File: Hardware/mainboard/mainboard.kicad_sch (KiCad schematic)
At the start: 85 parts, among them IC1 DS1813, IC2 DS1813, J1 Barrel_Jack, J2 Conn_02x02_Odd_Even, J3 Conn_01x06, J4 Conn_01x14, SW1 SW, U1 74AC161, U2 L7905, U4 PAL24, U5 GAL16V8, U6 W65C02SxP, U7 HM62256BLP, U8 28C256, U9 W65C51NxP, X1 24MHz, X3 1.8432MHz

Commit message: Fix mainboard power + add A13 and A14 to RAM/ROM address decoding.
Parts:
- removed U2: L7905, Package_TO_SOT_THT:TO-220-3_Vertical, symbol Regulator_Linear:L7905
- added C3, C4: .1u, Capacitor_THT:C_Disc_D4.3mm_W1.9mm_P5.00mm, symbol Device:C_Small
- added C5: 47u, Capacitor_THT:CP_Radial_D4.0mm_P2.00mm, symbol Device:C_Small
- added U1: L7805, Package_TO_SOT_THT:TO-220-3_Vertical, symbol Regulator_Linear:L7805
- C1: renamed from C13; footprint Capacitor_THT:CP_Radial_D6.3mm_P2.50mm -> Capacitor_THT:CP_Radial_D4.0mm_P2.00mm
- C12: renamed from C6; value 47n -> 1u
- R25: renamed from R27; footprint Resistor_THT:R_Axial_DIN0204_L3.6mm_D1.6mm_P5.08mm_Horizontal -> Resistor_THT:R_Axial_DIN0207_L6.3mm_D2.5mm_P7.62mm_Horizontal
- U2: renamed from U4; value PAL24 -> AT22V10
- renumbered C16 to C10, C7 to C11, C4 to C13, C17 to C14, C12 to C15, C8 to C16, C2 to C17, C15 to C18, C5 to C19, C1 to C2, C9 to C20, C10 to C6, C3 to C7, C11 to C8, C14 to C9, D9 to D1, D1 to D3, D3 to D4, D4 to D5, D5 to D6, D6 to D7, D7 to D8, D8 to D9, H5 to H1, H6 to H2, H1 to H3, H2 to H4, H3 to H5, J3 to J2, J2 to J3, R10 to R1, R4 to R10, R5 to R11, R6 to R12, R14 to R13, R21 to R14, R22 to R15, R7 to R16, R16 to R17, R15 to R18, R24 to R19, R11 to R2, R25 to R20, R26 to R21, R17 to R22, R18 to R23, R23 to R24, R12 to R3, R13 to R4, R9 to R5, R1 to R6, R8 to R7, R2 to R8, R3 to R9, SLOT4 to SLOT1, SLOT0 to SLOT2, SLOT1 to SLOT3, SLOT5 to SLOT4, SLOT2 to SLOT5, SLOT3 to SLOT6, U9 to U3, U7 to U4, U1 to U5, U8 to U6, U5 to U7, U6 to U8, X3 to X2
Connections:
- net +5V: now also C4.1, C5.1, U1.3 (OUT); no longer C1.1
- net A13: now also U7.15 (IO5)
- net A14: now also U7.14 (IO6)
- net GND: now also C3.2, C4.2, C5.2, U1.2 (GND)
- net at D1.1 (K), SW1.1 (A): now also C1.1
- net at SW1.2 (B): now also C3.1, U1.1 (IN)
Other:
- moved on the sheet: C1

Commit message: Change slot solder mask
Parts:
- renumbered SLOT2 to SLOT0, SLOT3 to SLOT1, SLOT5 to SLOT2, SLOT6 to SLOT3, SLOT1 to SLOT4, SLOT4 to SLOT5
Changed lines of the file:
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@@
   (symbol (lib_id "Connector_Generic:Conn_02x25_Odd_Even") (at 172.72 91.44 0) (unit 1)
     (in_bom yes) (on_board yes)
-    (property "Reference" "SLOT5" (id 0) (at 173.99 55.4482 0))
+    (property "Reference" "SLOT2" (id 0) (at 173.99 55.4482 0))
     (property "Value" "Conn_01x40" (id 1) (at 173.99 57.7596 0))
     (property "Footprint" "Connector_PinSocket_2.54mm:PinSocket_2x25_P2.54mm_Vertical" (id 2) (at 172.72 91.44 0)
@@
   (symbol (lib_id "Connector_Generic:Conn_02x25_Odd_Even") (at 62.23 208.28 0) (unit 1)
     (in_bom yes) (on_board yes)
-    (property "Reference" "SLOT1" (id 0) (at 63.5 172.2882 0))
+    (property "Reference" "SLOT4" (id 0) (at 63.5 172.2882 0))
     (property "Value" "Conn_01x40" (id 1) (at 63.5 174.5996 0))
     (property "Footprint" "Connector_PinSocket_2.54mm:PinSocket_2x25_P2.54mm_Vertical" (id 2) (at 62.23 208.28 0)
@@
   (symbol (lib_id "Connector_Generic:Conn_02x25_Odd_Even") (at 118.11 209.55 0) (unit 1)
     (in_bom yes) (on_board yes)
-    (property "Reference" "SLOT4" (id 0) (at 119.38 173.5582 0))
+    (property "Reference" "SLOT5" (id 0) (at 119.38 173.5582 0))
     (property "Value" "Conn_01x40" (id 1) (at 119.38 175.8696 0))
     (property "Footprint" "Connector_PinSocket_2.54mm:PinSocket_2x25_P2.54mm_Vertical" (id 2) (at 118.11 209.55 0)
@@
   (symbol (lib_id "Connector_Generic:Conn_02x25_Odd_Even") (at 114.3 90.17 0) (unit 1)
     (in_bom yes) (on_board yes)
-    (property "Reference" "SLOT3" (id 0) (at 115.57 54.1782 0))
+    (property "Reference" "SLOT1" (id 0) (at 115.57 54.1782 0))
     (property "Value" "Conn_01x40" (id 1) (at 115.57 56.4896 0))
     (property "Footprint" "Connector_PinSocket_2.54mm:PinSocket_2x25_P2.54mm_Vertical" (id 2) (at 114.3 90.17 0)
@@
   (symbol (lib_id "Connector_Generic:Conn_02x25_Odd_Even") (at 234.95 91.44 0) (unit 1)
     (in_bom yes) (on_board yes)
-    (property "Reference" "SLOT6" (id 0) (at 236.22 55.4482 0))
+    (property "Reference" "SLOT3" (id 0) (at 236.22 55.4482 0))
     (property "Value" "Conn_01x40" (id 1) (at 236.22 57.7596 0))
     (property "Footprint" "Connector_PinSocket_2.54mm:PinSocket_2x25_P2.54mm_Vertical" (id 2) (at 234.95 91.44 0)
@@
   (symbol (lib_id "Connector_Generic:Conn_02x25_Odd_Even") (at 63.5 90.17 0) (unit 1)
     (in_bom yes) (on_board yes)
-    (property "Reference" "SLOT2" (id 0) (at 64.77 54.1782 0))
+    (property "Reference" "SLOT0" (id 0) (at 64.77 54.1782 0))
     (property "Value" "Conn_01x40" (id 1) (at 64.77 56.4896 0))
     (property "Footprint" "Connector_PinSocket_2.54mm:PinSocket_2x25_P2.54mm_Vertical" (id 2) (at 63.5 90.17 0)
@@
       (reference "RESET1") (unit 1) (value "SW_Push") (footprint "Button_Switch_THT:SW_PUSH_6mm")
     )
+    (path "/00000000-0000-0000-0000-000060434fc0"
+      (reference "SLOT0") (unit 1) (value "Conn_01x40") (footprint "Connector_PinSocket_2.54mm:PinSocket_2x25_P2.54mm_Vertical")
+    )
+    (path "/00000000-0000-0000-0000-00005ff4ad1b"
+      (reference "SLOT1") (unit 1) (value "Conn_01x40") (footprint "Connector_PinSocket_2.54mm:PinSocket_2x25_P2.54mm_Vertical")
+    )
+    (path "/00000000-0000-0000-0000-00005ff330aa"
+      (reference "SLOT2") (unit 1) (value "Conn_01x40") (footprint "Connector_PinSocket_2.54mm:PinSocket_2x25_P2.54mm_Vertical")
+    )
+    (path "/00000000-0000-0000-0000-00005ff52d4f"
+      (reference "SLOT3") (unit 1) (value "Conn_01x40") (footprint "Connector_PinSocket_2.54mm:PinSocket_2x25_P2.54mm_Vertical")
+    )
     (path "/00000000-0000-0000-0000-00005ff388f3"
-      (reference "SLOT1") (unit 1) (value "Conn_01x40") (footprint "Connector_PinSocket_2.54mm:PinSocket_2x25_P2.54mm_Vertical")
-    )
-    (path "/00000000-0000-0000-0000-000060434fc0"
-      (reference "SLOT2") (unit 1) (value "Conn_01x40") (footprint "Connector_PinSocket_2.54mm:PinSocket_2x25_P2.54mm_Vertical")
-    )
-    (path "/00000000-0000-0000-0000-00005ff4ad1b"
-      (reference "SLOT3") (unit 1) (value "Conn_01x40") (footprint "Connector_PinSocket_2.54mm:PinSocket_2x25_P2.54mm_Vertical")
+      (reference "SLOT4") (unit 1) (value "Conn_01x40") (footprint "Connector_PinSocket_2.54mm:PinSocket_2x25_P2.54mm_Vertical")
     )
     (path "/00000000-0000-0000-0000-00005ff3d28d"
-      (reference "SLOT4") (unit 1) (value "Conn_01x40") (footprint "Connector_PinSocket_2.54mm:PinSocket_2x25_P2.54mm_Vertical")
-    )
-    (path "/00000000-0000-0000-0000-00005ff330aa"
       (reference "SLOT5") (unit 1) (value "Conn_01x40") (footprint "Connector_PinSocket_2.54mm:PinSocket_2x25_P2.54mm_Vertical")
     )
-    (path "/00000000-0000-0000-0000-00005ff52d4f"
-      (reference "SLOT6") (unit 1) (value "Conn_01x40") (footprint "Connector_PinSocket_2.54mm:PinSocket_2x25_P2.54mm_Vertical")
-    )
     (path "/00000000-0000-0000-0000-000060031505"

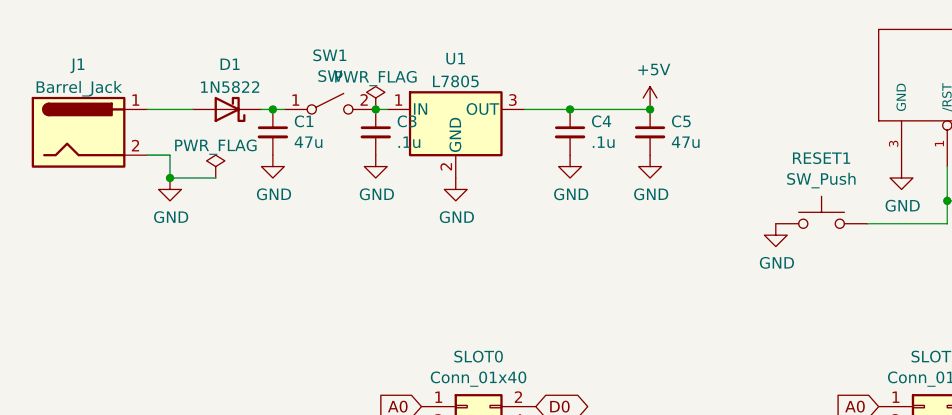
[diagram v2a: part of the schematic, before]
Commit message: Fix mainboard DRC
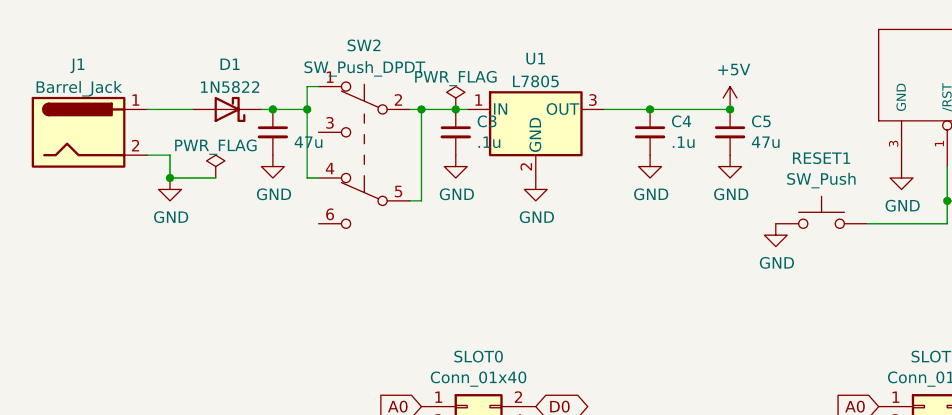
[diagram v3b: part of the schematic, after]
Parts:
- removed SW1: SW, Button_Switch_THT:SW_E-Switch_EG1271_SPDT, symbol Switch:SW_SPST
- added SW2: SW_Push_DPDT, Button_Switch_THT:SW_E-Switch_EG1271_SPDT, symbol Switch:SW_Push_DPDT
- IC1: footprint Package_TO_SOT_THT:TO-92L_Inline -> Package_TO_SOT_THT:TO-92_Inline_Wide
- IC2: footprint Package_TO_SOT_THT:TO-92_Inline -> Package_TO_SOT_THT:TO-92_Inline_Wide
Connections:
- net at C1.1, D1.1 (K): now also SW2.1 (A), SW2.4 (A)
- net at C3.1, U1.1 (IN): now also SW2.2 (B), SW2.5 (B)
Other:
- moved on the sheet: C3, C4, C5, U1
